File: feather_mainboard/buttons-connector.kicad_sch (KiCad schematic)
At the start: 0 parts

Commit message: finished daughter board
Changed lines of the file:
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@@
 	(wire
 		(pts
-			(xy 152.4 62.23) (xy 165.1 62.23)
+			(xy 144.78 87.63) (xy 157.48 87.63)
 		)
 		(stroke
@@
 	(wire
 		(pts
-			(xy 152.4 50.8) (xy 165.1 50.8)
+			(xy 144.78 76.2) (xy 157.48 76.2)
 		)
 		(stroke
@@
 	(wire
 		(pts
-			(xy 152.4 54.61) (xy 165.1 54.61)
+			(xy 144.78 80.01) (xy 157.48 80.01)
 		)
 		(stroke
@@
 	(wire
 		(pts
-			(xy 152.4 58.42) (xy 165.1 58.42)
+			(xy 144.78 83.82) (xy 157.48 83.82)
 		)
 		(stroke
@@
 	(text "Connector"
 		(exclude_from_sim no)
-		(at 149.098 101.346 0)
+		(at 150.368 106.426 0)
 		(effects
 			(font
@@
 	(hierarchical_label "Button_4"
 		(shape bidirectional)
-		(at 152.4 62.23 180)
+		(at 144.78 87.63 180)
 		(fields_autoplaced yes)
 		(effects
@@
 	(hierarchical_label "Button_2"
 		(shape bidirectional)
-		(at 152.4 54.61 180)
+		(at 144.78 80.01 180)
 		(fields_autoplaced yes)
 		(effects
@@
 	(hierarchical_label "Button_3"
 		(shape bidirectional)
-		(at 152.4 58.42 180)
+		(at 144.78 83.82 180)
 		(fields_autoplaced yes)
 		(effects
@@
 	(hierarchical_label "Button_1"
 		(shape bidirectional)
-		(at 152.4 50.8 180)
+		(at 144.78 76.2 180)
 		(fields_autoplaced yes)
 		(effects

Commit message: finished mainboard design, need to do the routing
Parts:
- added J2: 61900619521, Custom footprints:61900619521, symbol 61900619521:61900619521
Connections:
- net Button_1: now also J2.6
- net Button_2: now also J2.5
- net Button_3: now also J2.4
- net Button_4: now also J2.3
- new net GND: J2.1
- new net VCC: J2.2
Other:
- note removed: "Connector"

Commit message: finished mainboard and daughterboard
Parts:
- removed J2: 61900619521, Custom footprints:61900619521, symbol 61900619521:61900619521
- added J2: 62501021721, Custom footprints:62501021721, symbol 6250XX21721_62501021721:6250XX21721_62501021721
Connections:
- net Button_1: now also J2.6
- net Button_2: now also J2.7
- net Button_3: now also J2.5
- net Button_4: now also J2.3
- net GND: now also J2.4
- net VCC: now also J2.8
- no-connect marks 0 -> 4

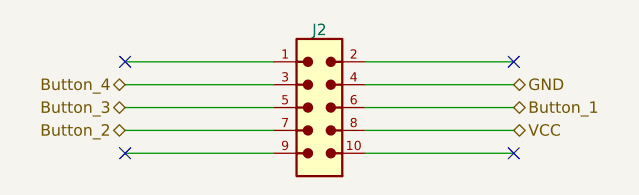
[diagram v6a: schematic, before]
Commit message: Updated the mainboard: removed unnecessary pull-ups on SD card lines; connected IIC pull-ups to enable circuit; cleaned up schematic
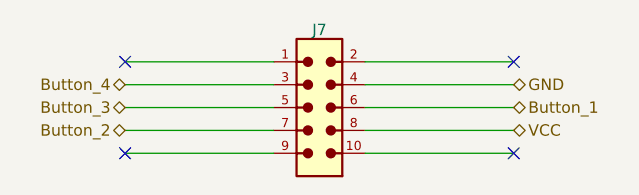
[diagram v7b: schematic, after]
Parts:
- J7: renamed from J2; footprint Custom footprints:62501021721 -> Custom footprints:62501021721_full
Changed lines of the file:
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@@
 		(shape bidirectional)
 		(at 173.99 96.52 0)
+		(fields_autoplaced yes)
 		(effects
 			(font
@@
 		(shape bidirectional)
 		(at 130.81 101.6 180)
+		(fields_autoplaced yes)
 		(effects
 			(font
@@
 		(shape bidirectional)
 		(at 130.81 99.06 180)
+		(fields_autoplaced yes)
 		(effects
 			(font
@@
 		(shape bidirectional)
 		(at 130.81 96.52 180)
+		(fields_autoplaced yes)
 		(effects
 			(font
@@
 		(shape bidirectional)
 		(at 173.99 99.06 0)
+		(fields_autoplaced yes)
 		(effects
 			(font
@@
 		(shape bidirectional)
 		(at 173.99 101.6 0)
+		(fields_autoplaced yes)
 		(effects
 			(font
@@
 		(on_board yes)
 		(dnp no)
-		(property "Reference" "J2"
+		(property "Reference" "J7"
 			(at 152.4 90.424 90)
 			(effects
@@
 			)
 		)
-		(property "Footprint" "Custom footprints:62501021721"
+		(property "Footprint" "Custom footprints:62501021721_full"
 			(at 152.4 99.06 0)
 			(effects
@@
 		(instances
 			(project "feather_mainboard"
-				(path "/e1e12730-ab4f-45db-8b66-c1e0f78e2f00/2182aea7-eb34-437a-b655-8b840f0aafa8"
-					(reference "J2")
+				(path "/e1e12730-ab4f-45db-8b66-c1e0f78e2f00/d8170bd3-ccd7-48c9-875f-738a35416792"
+					(reference "J7")
 					(unit 1)
 				)
